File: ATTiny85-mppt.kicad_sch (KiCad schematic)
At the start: 52 parts, among them J1 S+, J2 S-, J3 O+, J4 O-, Q1 BUK9511-55A127, Q2 BUK9511-55A127, Q3 2N2222A, Q4 2N2222A, Q5 2N2907A, Q6 2N2222A, Q7 2N2222A, SW1 Write OP-AMP DIFF, U1 LM7805_TO220, U2 LM358N, U3 ATtiny85-20PU

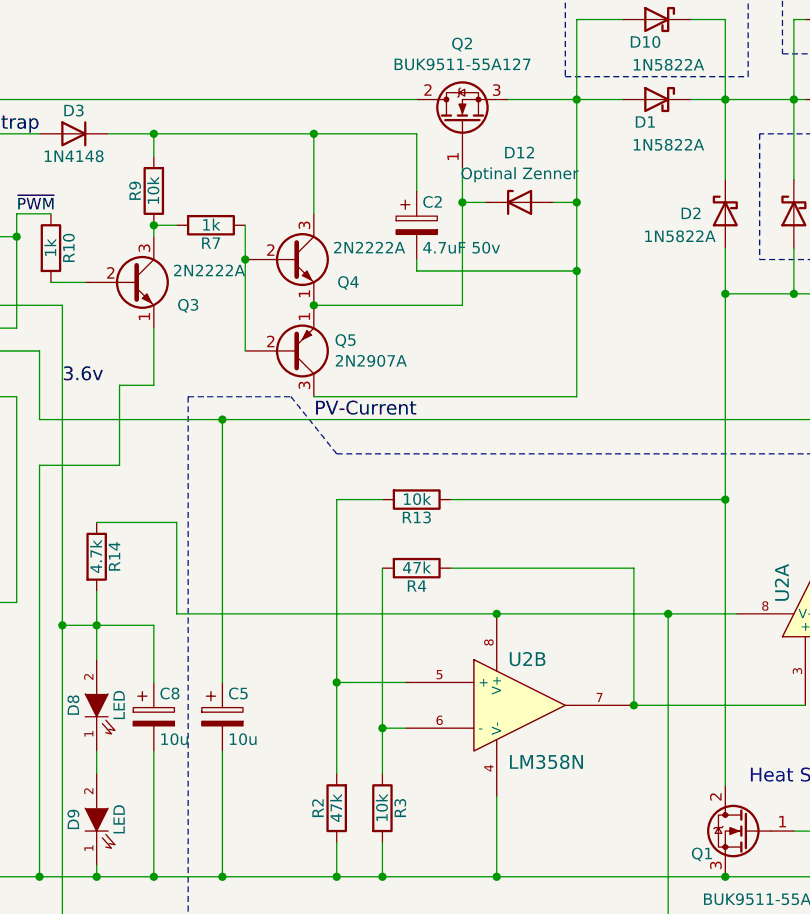
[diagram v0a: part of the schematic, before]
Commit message: Update capacitors.
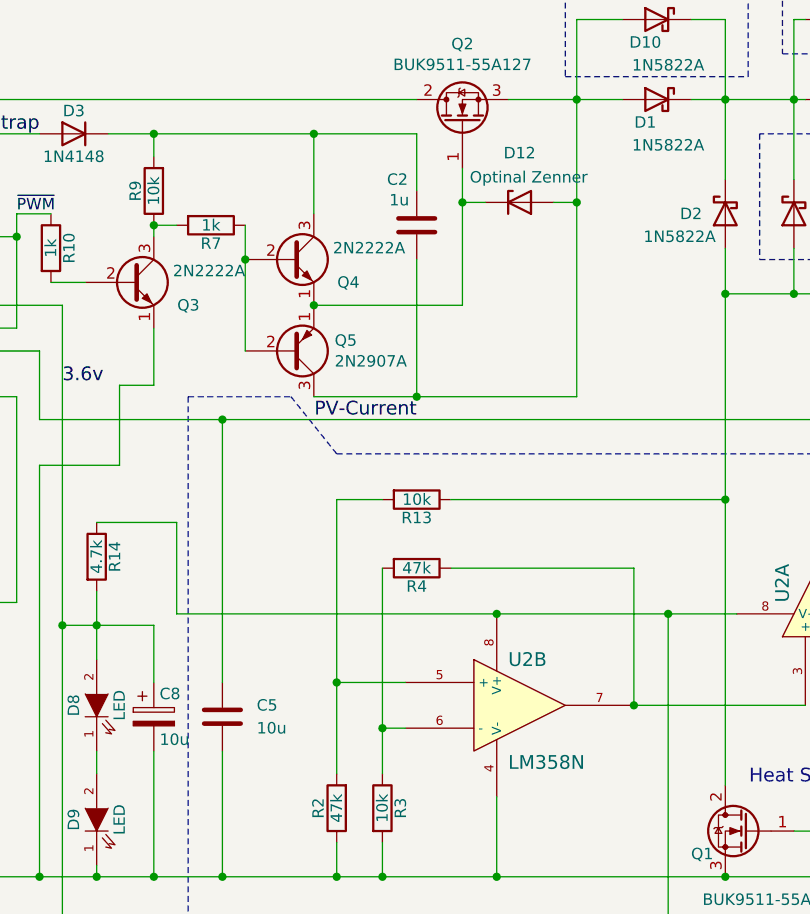
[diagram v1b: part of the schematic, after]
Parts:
- removed C2: 4.7uF 50v, Capacitors_THT:CP_Radial_D12.5mm_P5.00mm, symbol Device:CP
- removed C5: 10u, Capacitors_THT:CP_Radial_D12.5mm_P5.00mm, symbol Device:CP
- added C2: 1u, Capacitors_THT:C_Disc_D12.5mm_W5.0mm_P7.50mm, symbol Device:C
- added C5: 10u, Capacitors_THT:C_Disc_D12.5mm_W5.0mm_P7.50mm, symbol Device:C
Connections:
- net GND: now also C5.2
- net PV-Current: now also C5.1
- net at D1.2 (A), D10.2 (A), D12.2 (A)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: now also C2.2
- net at D3.1 (K), Q4.3 (C), R9.2: now also C2.1
